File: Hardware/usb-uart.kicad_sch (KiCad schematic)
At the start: 8 parts, among them J5 USB_C_Receptacle_USB2.0

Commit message: Maybe chad v3.0 hardware
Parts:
- R13: value 470 -> 5.1k

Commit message: RAE logo
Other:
- moved on the sheet: R11, R12
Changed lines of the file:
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@@
 	)
 	(junction
-		(at 125.73 96.52)
+		(at 128.27 95.25)
 		(diameter 0)
 		(color 0 0 0 0)
@@
 	(wire
 		(pts
-			(xy 118.11 96.52) (xy 118.11 99.06)
+			(xy 118.11 96.52) (xy 118.11 97.79)
 		)
 		(stroke
@@
 	(wire
 		(pts
-			(xy 125.73 93.98) (xy 125.73 96.52)
+			(xy 128.27 92.71) (xy 128.27 95.25)
 		)
 		(stroke
@@
 	(wire
 		(pts
-			(xy 115.57 93.98) (xy 120.65 93.98)
-		)
-		(stroke
-			(width 0)
-			(type default)
-		)
-	)
-	(wire
-		(pts
-			(xy 125.73 99.06) (xy 125.73 96.52)
+			(xy 128.27 92.71) (xy 125.73 92.71)
+		)
+		(stroke
+			(width 0)
+			(type default)
+		)
+	)
+	(wire
+		(pts
+			(xy 118.11 92.71) (xy 118.11 93.98)
+		)
+		(stroke
+			(width 0)
+			(type default)
+		)
+	)
+	(wire
+		(pts
+			(xy 118.11 92.71) (xy 120.65 92.71)
+		)
+		(stroke
+			(width 0)
+			(type default)
+		)
+	)
+	(wire
+		(pts
+			(xy 128.27 97.79) (xy 128.27 95.25)
 		)
 		(stroke
@@
 	(wire
 		(pts
-			(xy 125.73 96.52) (xy 127 96.52)
+			(xy 128.27 97.79) (xy 125.73 97.79)
+		)
+		(stroke
+			(width 0)
+			(type default)
+		)
+	)
+	(wire
+		(pts
+			(xy 128.27 95.25) (xy 130.81 95.25)
 		)
 		(stroke
@@
 	(wire
 		(pts
+			(xy 118.11 93.98) (xy 115.57 93.98)
+		)
+		(stroke
+			(width 0)
+			(type default)
+		)
+	)
+	(wire
+		(pts
 			(xy 115.57 107.95) (xy 116.84 107.95)
 		)
@@
 	(wire
 		(pts
-			(xy 118.11 99.06) (xy 120.65 99.06)
+			(xy 118.11 97.79) (xy 120.65 97.79)
 		)
 		(stroke
@@
 	(symbol
 		(lib_id "power:GND")
-		(at 127 96.52 90)
+		(at 130.81 95.25 90)
 		(unit 1)
 		(exclude_from_sim no)
@@
 		(dnp no)
 		(property "Reference" "#PWR037"
-			(at 133.35 96.52 0)
+			(at 137.16 95.25 0)
 			(effects
 				(font
@@
 		)
 		(property "Value" "GND"
-			(at 130.2512 96.393 90)
+			(at 134.0612 95.123 90)
 			(effects
 				(font
@@
 		)
 		(property "Footprint" ""
-			(at 127 96.52 0)
+			(at 130.81 95.25 0)
 			(effects
 				(font
@@
 		)
 		(property "Datasheet" ""
-			(at 127 96.52 0)
+			(at 130.81 95.25 0)
 			(effects
 				(font
@@
 		)
 		(property "Description" ""
-			(at 127 96.52 0)
+			(at 130.81 95.25 0)
 			(effects
 				(font
@@
 	(symbol
 		(lib_id "Device:R_Small")
-		(at 123.19 99.06 270)
+		(at 123.19 97.79 270)
 		(unit 1)
 		(exclude_from_sim no)
@@
 		(dnp no)
 		(property "Reference" "R12"
-			(at 129.54 100.33 90)
+			(at 127.254 99.5426 90)
 			(effects
 				(font
@@
 		)
 		(property "Value" "5.1k"
-			(at 129.54 102.6414 90)
+			(at 127.254 101.854 90)
 			(effects
 				(font
@@
 		)
 		(property "Footprint" "Resistor_SMD:R_0402_1005Metric"
-			(at 123.19 99.06 0)
+			(at 123.19 97.79 0)
 			(effects
 				(font
@@
 		)
 		(property "Datasheet" "~"
-			(at 123.19 99.06 0)
+			(at 123.19 97.79 0)
 			(effects
 				(font
@@
 		)
 		(property "Description" ""
-			(at 123.19 99.06 0)
+			(at 123.19 97.79 0)
 			(effects
 				(font
@@
 	(symbol
 		(lib_id "Device:R_Small")
-		(at 123.19 93.98 90)
+		(at 123.19 92.71 90)
 		(unit 1)
 		(exclude_from_sim no)
@@
 		(dnp no)
 		(property "Reference" "R11"
-			(at 123.19 89.0016 90)
+			(at 123.19 87.7316 90)
 			(effects
 				(font
@@
 		)
 		(property "Value" "5.1k"
-			(at 123.19 91.313 90)
+			(at 123.19 90.043 90)
 			(effects
 				(font
@@
 		)
 		(property "Footprint" "Resistor_SMD:R_0402_1005Metric"
-			(at 123.19 93.98 0)
+			(at 123.19 92.71 0)
 			(effects
 				(font
@@
 		)
 		(property "Datasheet" "~"
-			(at 123.19 93.98 0)
+			(at 123.19 92.71 0)
 			(effects
 				(font
@@
 		)
 		(property "Description" ""
-			(at 123.19 93.98 0)
-			(effects
-				(font
+			(at 123.19 92.71 0)
+			(effects
+				(font

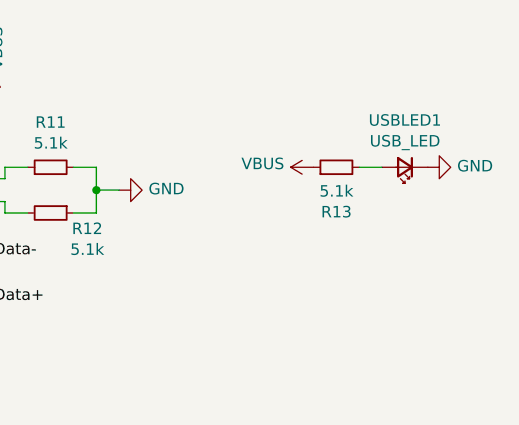
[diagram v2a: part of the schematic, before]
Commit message: 30V compatibility update
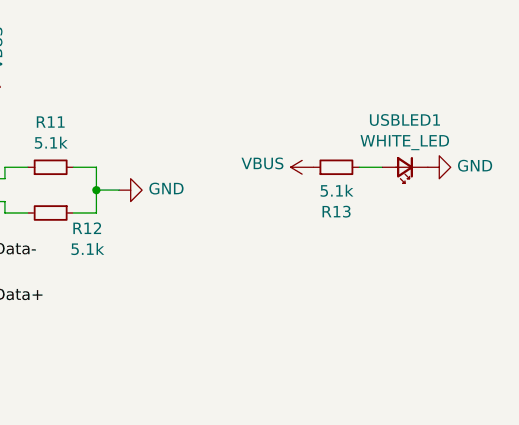
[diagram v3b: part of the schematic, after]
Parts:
- J5: footprint Connector_USB:USB_C_Receptacle_Palconn_UTC16-G -> iclr:USB_C_Receptacle_Palconn_UTC16-G
- USBLED1: value USB_LED -> WHITE_LED
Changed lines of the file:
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@@
 			)
 		)
-		(property "Footprint" "Connector_USB:USB_C_Receptacle_Palconn_UTC16-G"
+		(property "Footprint" "iclr:USB_C_Receptacle_Palconn_UTC16-G"
 			(at 104.14 104.14 0)
 			(effects
@@
 			)
 		)
-		(property "Value" "USB_LED"
+		(property "Value" "WHITE_LED"
 			(at 162.56 89.8144 0)
 			(effects

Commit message: cleaned up schematic and bom
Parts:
- D302: renamed from USBLED1; value WHITE_LED -> LED_WHITE
- R301: renamed from R11; value 5.1k -> 5.1kΩ
- R302: renamed from R12; value 5.1k -> 5.1kΩ
- R303: renamed from R13; value 5.1k -> 5.1kΩ
- TP301: renamed from TP1; now left out of the parts list
- TP302: renamed from TP2; now left out of the parts list
- renumbered D2 to D301, J5 to J301
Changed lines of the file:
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@@
 (kicad_sch
-	(version 20231120)
+	(version 20250114)
 	(generator "eeschema")
-	(generator_version "8.0")
+	(generator_version "9.0")
 	(paper "A4")
 	(junction
@@
 	(wire
 		(pts
+			(xy 167.64 92.71) (xy 165.1 92.71)
+		)
+		(stroke
+			(width 0)
+			(type default)
+		)
+	)
+	(wire
+		(pts
 			(xy 160.02 92.71) (xy 157.48 92.71)
 		)
@@
 	(wire
 		(pts
+			(xy 167.64 95.25) (xy 167.64 92.71)
+		)
+		(stroke
+			(width 0)
+			(type default)
+		)
+	)
+	(wire
+		(pts
 			(xy 118.11 92.71) (xy 118.11 93.98)
 		)
@@
 	(wire
 		(pts
+			(xy 148.59 92.71) (xy 152.4 92.71)
+		)
+		(stroke
+			(width 0)
+			(type default)
+		)
+	)
+	(wire
+		(pts
 			(xy 118.11 92.71) (xy 120.65 92.71)
 		)
@@
 		(pts
 			(xy 116.84 88.9) (xy 115.57 88.9)
+		)
+		(stroke
+			(width 0)
+			(type default)
+		)
+	)
+	(wire
+		(pts
+			(xy 148.59 92.71) (xy 148.59 90.17)
 		)
 		(stroke
@@
 	(label "Data+"
 		(at 44.45 104.14 0)
-		(fields_autoplaced yes)
 		(effects
 			(font
@@
 	(label "Data+"
 		(at 132.08 134.62 90)
-		(fields_autoplaced yes)
 		(effects
 			(font
@@
 	(label "Data-"
 		(at 44.45 99.06 0)
-		(fields_autoplaced yes)
 		(effects
 			(font
@@
 	(label "Data-"
 		(at 116.84 102.87 0)
-		(fields_autoplaced yes)
 		(effects
 			(font
@@
 	(label "Data+"
 		(at 116.84 107.95 0)
-		(fields_autoplaced yes)
 		(effects
 			(font
@@
 	(label "VBUS"
 		(at 134.62 134.62 90)
-		(fields_autoplaced yes)
 		(effects
 			(font
@@
 	(label "Data-"
 		(at 129.54 134.62 90)
-		(fields_autoplaced yes)
 		(effects
 			(font
@@
 		(shape bidirectional)
 		(at 44.45 99.06 180)
-		(fields_autoplaced yes)
 		(effects
 			(font
@@
 		(shape bidirectional)
 		(at 44.45 104.14 180)
-		(fields_autoplaced yes)
 		(effects
 			(font
@@
 		(on_board yes)
 		(dnp no)
-		(property "Reference" "#PWR037"
+		(property "Reference" "#PWR0303"
 			(at 137.16 95.25 0)
 			(effects
@@
 			(project "Chad"
 				(path "/7db990e4-92e1-4f99-b4d2-435bbec1ba83/00000000-0000-0000-0000-000061925999"
-					(reference "#PWR037")
+					(reference "#PWR0303")
 					(unit 1)
 				)
@@
 		(on_board yes)
 		(dnp no)
-		(property "Reference" "R12"
+		(property "Reference" "R302"
 			(at 127.254 99.5426 90)
 			(effects
@@
 			)
 		)
-		(property "Value" "5.1k"
+		(property "Value" "5.1kΩ"
 			(at 127.254 101.854 90)
 			(effects
@@
 			(project "Chad"
 				(path "/7db990e4-92e1-4f99-b4d2-435bbec1ba83/00000000-0000-0000-0000-000061925999"
-					(reference "R12")
+					(reference "R302")
 					(unit 1)
 				)
@@
 		(on_board yes)
 		(dnp no)
-		(property "Reference" "R11"
+		(property "Reference" "R301"
 			(at 123.19 87.7316 90)
 			(effects
@@
 			)
 		)
-		(property "Value" "5.1k"
+		(property "Value" "5.1kΩ"
 			(at 123.19 90.043 90)
 			(effects
@@
 			(project "Chad"
 				(path "/7db990e4-92e1-4f99-b4d2-435bbec1ba83/00000000-0000-0000-0000-000061925999"
-					(reference "R11")
+					(reference "R301")
 					(unit 1)
 				)
@@
 		(on_board yes)
 		(dnp no)
-		(property "Reference" "#PWR035"
+		(property "Reference" "#PWR0301"
 			(at 96.52 137.16 0)
 			(effects
@@
 			(project "Chad"
 				(path "/7db990e4-92e1-4f99-b4d2-435bbec1ba83/00000000-0000-0000-0000-000061925999"
-					(reference "#PWR035")
+					(reference "#PWR0301")
 					(unit 1)
 				)
@@
 		(on_board yes)
 		(dnp no)
-		(property "Reference" "J5"
+		(property "Reference" "J301"
 			(at 103.0478 82.1182 0)
 			(effects
@@
 			(project "Chad"
 				(path "/7db990e4-92e1-4f99-b4d2-435bbec1ba83/00000000-0000-0000-0000-000061925999"
-					(reference "J5")
+					(reference "J301")
 					(unit 1)
 				)
@@
 		(on_board yes)
 		(dnp no)
-		(property "Reference" "#PWR038"
+		(property "Reference" "#PWR0304"
 			(at 132.08 151.13 0)
 			(effects
@@
 			(project "Chad"
 				(path "/7db990e4-92e1-4f99-b4d2-435bbec1ba83/00000000-0000-0000-0000-000061925999"
-					(reference "#PWR038")
+					(reference "#PWR0304")
 					(unit 1)
 				)
@@
 		(on_board yes)
 		(dnp no)
-		(property "Reference" "D2"
+		(property "Reference" "D301"
 			(at 137.287 138.5316 0)
 			(effects
@@
 			(project "Chad"
 				(path "/7db990e4-92e1-4f99-b4d2-435bbec1ba83/00000000-0000-0000-0000-000061925999"
-					(reference "D2")
+					(reference "D301")
 					(unit 1)
 				)
@@
 		(on_board yes)
 		(dnp no)
-		(property "Reference" "#PWR036"
+		(property "Reference" "#PWR0302"
 			(at 116.84 88.9 0)
 			(effects
@@
 			(project "Chad"
 				(path "/7db990e4-92e1-4f99-b4d2-435bbec1ba83/00000000-0000-0000-0000-000061925999"
-					(reference "#PWR036")
+					(reference "#PWR0302")
 					(unit 1)
 				)
@@
 		(unit 1)
 		(exclude_from_sim no)
-		(in_bom yes)
+		(in_bom no)
 		(on_board yes)
 		(dnp no)
-		(property "Reference" "TP1"
+		(property "Reference" "TP301"
 			(at 56.8452 97.8916 90)
 			(effects
@@
 			(project "Chad"
 				(path "/7db990e4-92e1-4f99-b4d2-435bbec1ba83/00000000-0000-0000-0000-000061925999"
-					(reference "TP1")
+					(reference "TP301")
 					(unit 1)
 				)
@@
 		(unit 1)
 		(exclude_from_sim no)
-		(in_bom yes)
+		(in_bom no)
 		(on_board yes)
 		(dnp no)
-		(property "Reference" "TP2"
+		(property "Reference" "TP302"
 			(at 56.8452 102.9716 90)
 			(effects
@@
 			(project "Chad"
 				(path "/7db990e4-92e1-4f99-b4d2-435bbec1ba83/00000000-0000-0000-0000-000061925999"
-					(reference "TP2")
+					(reference "TP302")
 					(unit 1)
 				)
@@
 		(on_board yes)
 		(dnp no)
-		(property "Reference" "USBLED1"
+		(property "Reference" "D302"
 			(at 162.56 87.503 0)
 			(effects
@@
 			)
 		)
-		(property "Value" "WHITE_LED"
+		(property "Value" "LED_WHITE"
 			(at 162.56 89.8144 0)
 			(effects
@@
 			(project "Chad"
 				(path "/7db990e4-92e1-4f99-b4d2-435bbec1ba83/00000000-0000-0000-0000-000061925999"
-					(reference "USBLED1")
+					(reference "D302")
 					(unit 1)
 				)
@@
 		(on_board yes)
 		(dnp no)
-		(property "Reference" "R13"
+		(property "Reference" "R303"
 			(at 154.94 97.6884 90)
 			(effects
@@
 			)
 		)
-		(property "Value" "5.1k"
+		(property "Value" "5.1kΩ"
 			(at 154.94 95.377 90)
 			(effects
@@
 			(project "Chad"
 				(path "/7db990e4-92e1-4f99-b4d2-435bbec1ba83/00000000-0000-0000-0000-000061925999"
-					(reference "R13")
+					(reference "R303")
 					(unit 1)
 				)
@@
 	(symbol
 		(lib_id "power:GND")
-		(at 165.1 92.71 90)
+		(at 167.64 95.25 0)
 		(unit 1)
 		(exclude_from_sim no)
@@
 		(on_board yes)
 		(dnp no)
-		(property "Reference" "#PWR040"
-			(at 171.45 92.71 0)
+		(property "Reference" "#PWR0306"
+			(at 167.64 101.6 0)
 			(effects
 				(font
@@
 		)
 		(property "Value" "GND"
-			(at 168.3512 92.583 90)
+			(at 167.767 98.5012 0)
 			(effects
 				(font
@@
 		)
 		(property "Footprint" ""
-			(at 165.1 92.71 0)
+			(at 167.64 95.25 0)
 			(effects
 				(font
@@
 		)
 		(property "Datasheet" ""
-			(at 165.1 92.71 0)
+			(at 167.64 95.25 0)
 			(effects
 				(font
@@
 		)
 		(property "Description" ""
-			(at 165.1 92.71 0)
+			(at 167.64 95.25 0)
 			(effects
 				(font
@@
 			(project "Chad"
 				(path "/7db990e4-92e1-4f99-b4d2-435bbec1ba83/00000000-0000-0000-0000-000061925999"
-					(reference "#PWR040")
+					(reference "#PWR0306")
 					(unit 1)
 				)
@@
 	(symbol
 		(lib_id "power:VBUS")
-		(at 152.4 92.71 90)
+		(at 148.59 90.17 0)
 		(unit 1)
 		(exclude_from_sim no)
@@
 		(on_board yes)
 		(dnp no)
-		(property "Reference" "#PWR039"
-			(at 156.21 92.71 0)
+		(property "Reference" "#PWR0305"
+			(at 148.59 93.98 0)
 			(effects
 				(font
@@
 		)
 		(property "Value" "VBUS"
-			(at 149.1488 92.329 90)
+			(at 148.971 86.9188 0)
 			(effects
 				(font
@@
 		)
 		(property "Footprint" ""
-			(at 152.4 92.71 0)
+			(at 148.59 90.17 0)
 			(effects
 				(font
@@
 		)
 		(property "Datasheet" ""
-			(at 152.4 92.71 0)
+			(at 148.59 90.17 0)
 			(effects
 				(font
@@
 		)
 		(property "Description" ""
-			(at 152.4 92.71 0)
+			(at 148.59 90.17 0)
 			(effects
 				(font
@@
 			(project "Chad"
 				(path "/7db990e4-92e1-4f99-b4d2-435bbec1ba83/00000000-0000-0000-0000-000061925999"
-					(reference "#PWR039")
+					(reference "#PWR0305")
 					(unit 1)
 				)
